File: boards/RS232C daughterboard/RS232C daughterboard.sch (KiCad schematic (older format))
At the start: 1 part

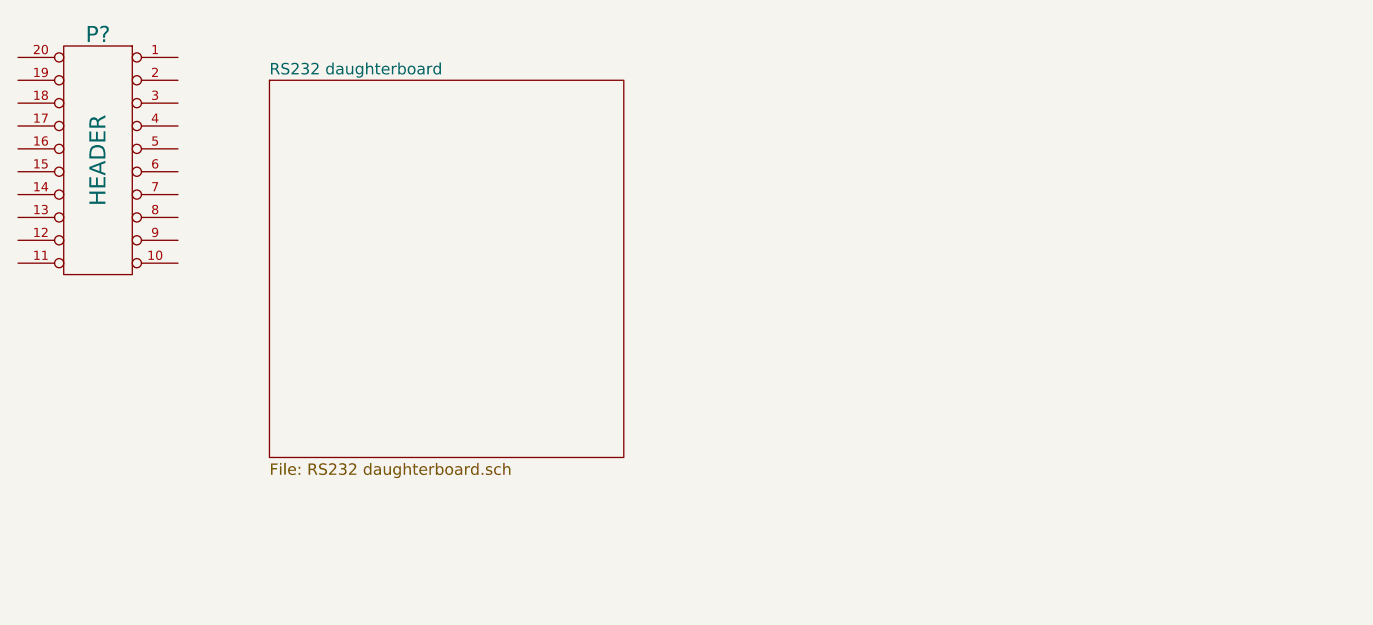
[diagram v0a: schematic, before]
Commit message: Filled in RS232 dboard, changed GPIO24 to GPIO16 board
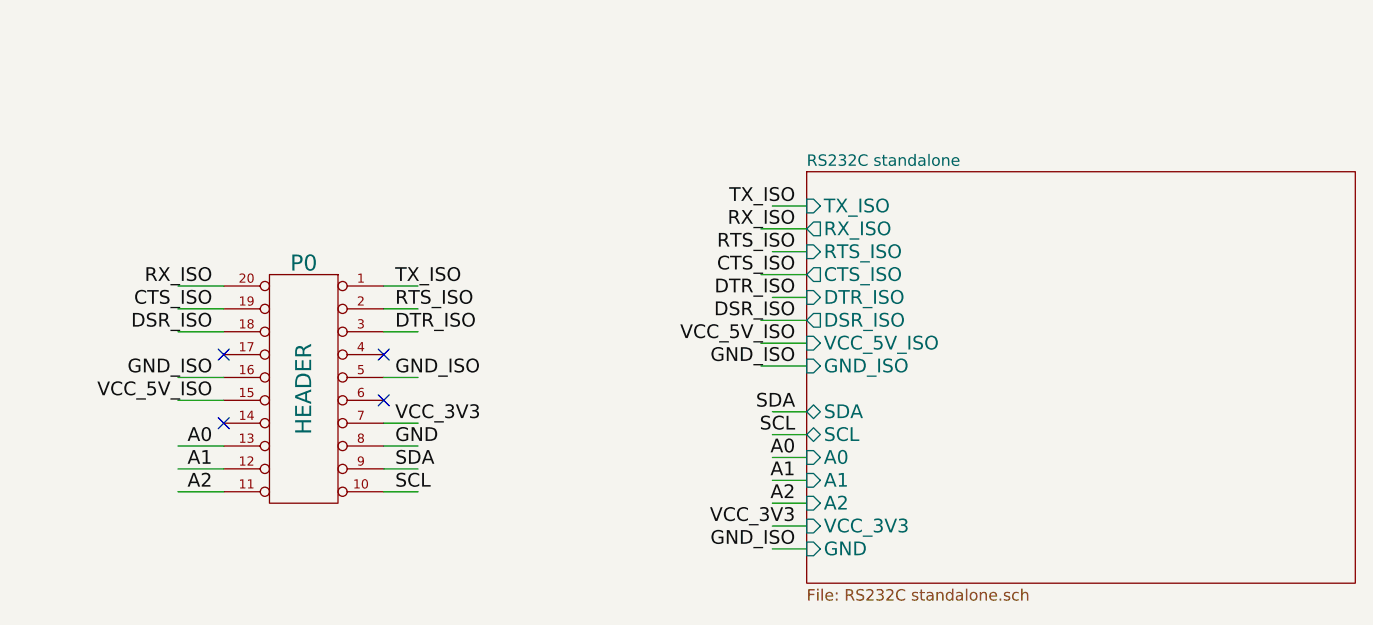
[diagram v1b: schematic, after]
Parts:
- removed P?: HEADER, symbol DIL20
- added P0: HEADER, symbol DIL20
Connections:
- net labels added: A0, A1, A2, CTS_ISO, DSR_ISO, DTR_ISO, GND, GND_ISO, RTS_ISO, RX_ISO, SCL, SDA, TX_ISO, VCC_3V3, VCC_5V_ISO
- wire segments 0 -> 31
- no-connect marks 0 -> 4
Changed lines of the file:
@@
 LIBS:CONN_16
 LIBS:csmall
+LIBS:ISL83387E
+LIBS:RS232C daughterboard-cache
 EELAYER 27 0
 EELAYER END
 $Descr A4 11693 8268
 encoding utf-8
-Sheet 1 1
+Sheet 1 2
 Title ""
 Date "26 jun 2014"
@@
 $EndDescr
 $Comp
-L DIL20 P?
-U 1 1 53AB657B
-P 2900 3300
-F 0 "P?" H 2900 3850 70  0000 C CNN
-F 1 "HEADER" V 2900 3300 70  0000 C CNN
-F 2 "" H 2900 3300 60  0000 C CNN
-F 3 "" H 2900 3300 60  0000 C CNN
-	1    2900 3300
+L DIL20 P0
+U 1 1 53AB69C0
+P 3800 4300
+F 0 "P0" H 3800 4850 70  0000 C CNN
+F 1 "HEADER" V 3800 4300 70  0000 C CNN
+F 2 "" H 3800 4300 60  0000 C CNN
+F 3 "" H 3800 4300 60  0000 C CNN
+	1    3800 4300
 	-1   0    0    -1
 $EndComp
 $Sheet
-S 3650 2950 1550 1650
-U 53AB65C8
-F0 "RS232 daughterboard" 50
-F1 "RS232 daughterboard.sch" 50
+S 6000 3350 2400 1800
+U 53AB69CE
+F0 "RS232C standalone" 50
+F1 "RS232C standalone.sch" 50
+F2 "TX_ISO" I L 6000 3500 60
+F3 "RX_ISO" O L 6000 3600 60
+F4 "RTS_ISO" I L 6000 3700 60
+F5 "CTS_ISO" O L 6000 3800 60
+F6 "DTR_ISO" I L 6000 3900 60
+F7 "DSR_ISO" O L 6000 4000 60
+F8 "VCC_3V3" I L 6000 4900 60
+F9 "GND" I L 6000 5000 60
+F10 "VCC_5V_ISO" I L 6000 4100 60
+F11 "GND_ISO" I L 6000 4200 60
+F12 "SDA" B L 6000 4400 60
+F13 "SCL" B L 6000 4500 60
+F14 "A0" I L 6000 4600 60
+F15 "A1" I L 6000 4700 60
+F16 "A2" I L 6000 4800 60
 $EndSheet
+Wire Wire Line
+	3450 3850 3250 3850
+Wire Wire Line
+	3450 3950 3250 3950
+Wire Wire Line
+	3450 4050 3250 4050
+Wire Wire Line
+	3450 4250 3250 4250
+Wire Wire Line
+	3450 4350 3250 4350
+Wire Wire Line
+	3450 4550 3250 4550
+Wire Wire Line
+	4300 3850 4150 3850
+Wire Wire Line
+	4300 3950 4150 3950
+Wire Wire Line
+	4300 4050 4150 4050
+Wire Wire Line
+	4300 4250 4150 4250
+Wire Wire Line
+	4300 4450 4150 4450
+Wire Wire Line
+	4300 4550 4150 4550
+Wire Wire Line
+	3450 4650 3250 4650
+Wire Wire Line
+	3450 4750 3250 4750
+Wire Wire Line
+	4300 4650 4150 4650
+Wire Wire Line
+	4300 4750 4150 4750
+Text Label 4200 3850 0    60   ~ 0
+TX_ISO
+Text Label 4200 3950 0    60   ~ 0
+RTS_ISO
+Text Label 4200 4050 0    60   ~ 0
+DTR_ISO
+Text Label 4200 4450 0    60   ~ 0
+VCC_3V3
+Text Label 4200 4550 0    60   ~ 0
+GND
+Text Label 4200 4650 0    60   ~ 0
+SDA
+Text Label 4200 4750 0    60   ~ 0
+SCL
+Text Label 3400 4750 2    60   ~ 0
+A2
+Text Label 3400 4650 2    60   ~ 0
+A1
+Text Label 3400 4550 2    60   ~ 0
+A0
+Text Label 3400 4350 2    60   ~ 0
+VCC_5V_ISO
+Text Label 3400 4250 2    60   ~ 0
+GND_ISO
+Text Label 3400 4050 2    60   ~ 0
+DSR_ISO
+Text Label 3400 3950 2    60   ~ 0
+CTS_ISO
+Text Label 3400 3850 2    60   ~ 0
+RX_ISO
+Text Label 4200 4250 0    60   ~ 0
+GND_ISO
+NoConn ~ 4150 4350
+NoConn ~ 4150 4150
+NoConn ~ 3450 4150
+NoConn ~ 3450 4450
+Wire Wire Line
+	6000 3600 5800 3600
+Text Label 5950 3600 2    60   ~ 0
+RX_ISO
+Wire Wire Line
+	6000 3800 5800 3800
+Text Label 5950 3800 2    60   ~ 0
+CTS_ISO
+Wire Wire Line
+	6000 4000 5800 4000
+Text Label 5950 4000 2    60   ~ 0
+DSR_ISO
+Wire Wire Line
+	5850 3500 6000 3500
+Text Label 5950 3500 2    60   ~ 0
+TX_ISO
+Wire Wire Line
+	5850 3700 6000 3700
+Wire Wire Line
+	5850 3900 6000 3900
+Text Label 5950 3700 2    60   ~ 0
+RTS_ISO
+Text Label 5950 3900 2    60   ~ 0
+DTR_ISO
+Wire Wire Line
+	6000 4100 5800 4100
+Text Label 5950 4100 2    60   ~ 0
+VCC_5V_ISO
+Wire Wire Line
+	6000 4200 5800 4200
+Text Label 5950 4200 2    60   ~ 0
+GND_ISO
+Wire Wire Line
+	6000 4600 5850 4600
+Wire Wire Line
+	6000 4700 5850 4700
+Wire Wire Line
+	6000 4800 5850 4800
+Text Label 5950 4800 2    60   ~ 0
+A2
+Text Label 5950 4700 2    60   ~ 0
+A1
+Text Label 5950 4600 2    60   ~ 0
+A0
+Wire Wire Line
+	5850 4400 6000 4400
+Wire Wire Line
+	5850 4500 6000 4500
+Text Label 5950 4400 2    60   ~ 0
+SDA
+Text Label 5950 4500 2    60   ~ 0
+SCL
+Wire Wire Line
+	5850 5000 6000 5000
+Text Label 5950 4900 2    60   ~ 0
+VCC_3V3
+Text Label 5950 5000 2    60   ~ 0
+GND_ISO
+Wire Wire Line
+	6000 4900 5850 4900
 $EndSCHEMATC

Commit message: Completed RS232C daughterboard
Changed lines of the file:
@@
 NoConn ~ 3450 4450
 Wire Wire Line
-	6000 3600 5800 3600
-Text Label 5950 3600 2    60   ~ 0
+	6000 3600 5850 3600
+Text Label 5850 3600 2    60   ~ 0
 RX_ISO
 Wire Wire Line
-	6000 3800 5800 3800
-Text Label 5950 3800 2    60   ~ 0
+	6000 3800 5850 3800
+Text Label 5850 3800 2    60   ~ 0
 CTS_ISO
 Wire Wire Line
-	6000 4000 5800 4000
-Text Label 5950 4000 2    60   ~ 0
+	6000 4000 5850 4000
+Text Label 5850 4000 2    60   ~ 0
 DSR_ISO
 Wire Wire Line
 	5850 3500 6000 3500
-Text Label 5950 3500 2    60   ~ 0
+Text Label 5850 3500 2    60   ~ 0
 TX_ISO
 Wire Wire Line
@@
 Wire Wire Line
 	5850 3900 6000 3900
-Text Label 5950 3700 2    60   ~ 0
+Text Label 5850 3700 2    60   ~ 0
 RTS_ISO
-Text Label 5950 3900 2    60   ~ 0
+Text Label 5850 3900 2    60   ~ 0
 DTR_ISO
 Wire Wire Line
-	6000 4100 5800 4100
-Text Label 5950 4100 2    60   ~ 0
+	6000 4100 5850 4100
+Text Label 5850 4100 2    60   ~ 0
 VCC_5V_ISO
 Wire Wire Line
-	6000 4200 5800 4200
-Text Label 5950 4200 2    60   ~ 0
+	6000 4200 5850 4200
+Text Label 5850 4200 2    60   ~ 0
 GND_ISO
 Wire Wire Line
@@
 Wire Wire Line
 	6000 4800 5850 4800
-Text Label 5950 4800 2    60   ~ 0
+Text Label 5850 4800 2    60   ~ 0
 A2
-Text Label 5950 4700 2    60   ~ 0
+Text Label 5850 4700 2    60   ~ 0
 A1
-Text Label 5950 4600 2    60   ~ 0
+Text Label 5850 4600 2    60   ~ 0
 A0
 Wire Wire Line
@@
 Wire Wire Line
 	5850 4500 6000 4500
-Text Label 5950 4400 2    60   ~ 0
+Text Label 5850 4400 2    60   ~ 0
 SDA
-Text Label 5950 4500 2    60   ~ 0
+Text Label 5850 4500 2    60   ~ 0
 SCL
 Wire Wire Line
 	5850 5000 6000 5000
-Text Label 5950 4900 2    60   ~ 0
+Text Label 5850 4900 2    60   ~ 0
 VCC_3V3
-Text Label 5950 5000 2    60   ~ 0
+Text Label 5850 5000 2    60   ~ 0
 GND_ISO
 Wire Wire Line

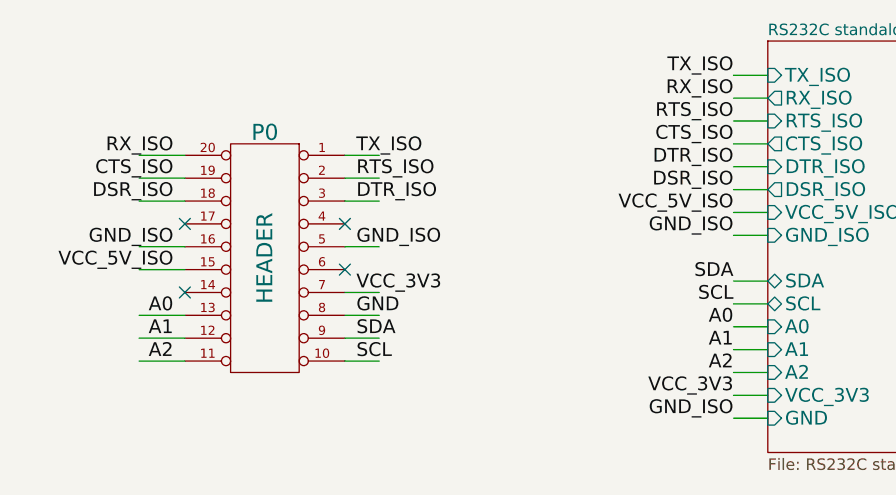
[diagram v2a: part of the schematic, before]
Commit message: Fixed errors in RS232C daughterboard, ERC passed
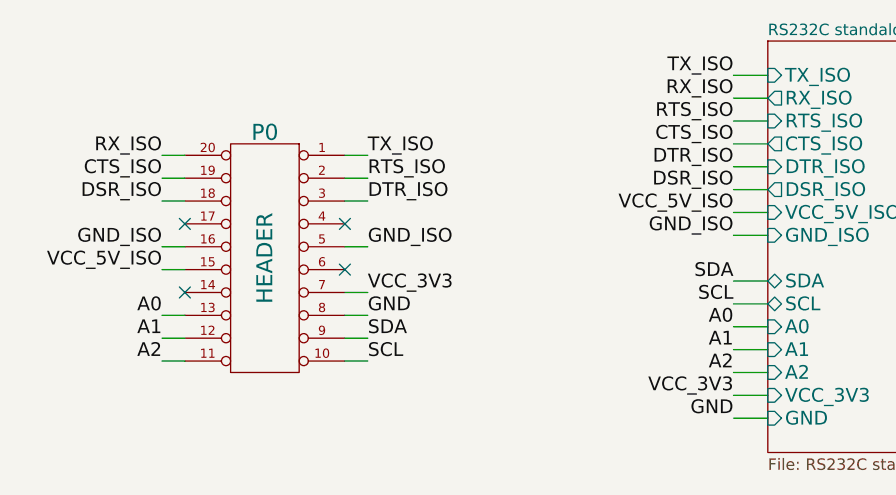
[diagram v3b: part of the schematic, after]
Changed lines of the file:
@@
 $EndSheet
 Wire Wire Line
-	3450 3850 3250 3850
+	3450 3850 3350 3850
 Wire Wire Line
-	3450 3950 3250 3950
+	3450 3950 3350 3950
 Wire Wire Line
-	3450 4050 3250 4050
+	3450 4050 3350 4050
 Wire Wire Line
-	3450 4250 3250 4250
+	3450 4250 3350 4250
 Wire Wire Line
-	3450 4350 3250 4350
+	3450 4350 3350 4350
 Wire Wire Line
-	3450 4550 3250 4550
+	3450 4550 3350 4550
 Wire Wire Line
-	4300 3850 4150 3850
+	4250 3850 4150 3850
 Wire Wire Line
-	4300 3950 4150 3950
+	4250 3950 4150 3950
 Wire Wire Line
-	4300 4050 4150 4050
+	4250 4050 4150 4050
 Wire Wire Line
-	4300 4250 4150 4250
+	4250 4250 4150 4250
 Wire Wire Line
-	4300 4450 4150 4450
+	4250 4450 4150 4450
 Wire Wire Line
-	4300 4550 4150 4550
+	4250 4550 4150 4550
 Wire Wire Line
-	3450 4650 3250 4650
+	3450 4650 3350 4650
 Wire Wire Line
-	3450 4750 3250 4750
+	3450 4750 3350 4750
 Wire Wire Line
-	4300 4650 4150 4650
+	4250 4650 4150 4650
 Wire Wire Line
-	4300 4750 4150 4750
-Text Label 4200 3850 0    60   ~ 0
+	4250 4750 4150 4750
+Text Label 4250 3850 0    60   ~ 0
 TX_ISO
-Text Label 4200 3950 0    60   ~ 0
+Text Label 4250 3950 0    60   ~ 0
 RTS_ISO
-Text Label 4200 4050 0    60   ~ 0
+Text Label 4250 4050 0    60   ~ 0
 DTR_ISO
-Text Label 4200 4450 0    60   ~ 0
+Text Label 4250 4450 0    60   ~ 0
 VCC_3V3
-Text Label 4200 4550 0    60   ~ 0
+Text Label 4250 4550 0    60   ~ 0
 GND
-Text Label 4200 4650 0    60   ~ 0
+Text Label 4250 4650 0    60   ~ 0
 SDA
-Text Label 4200 4750 0    60   ~ 0
+Text Label 4250 4750 0    60   ~ 0
 SCL
-Text Label 3400 4750 2    60   ~ 0
+Text Label 3350 4750 2    60   ~ 0
 A2
-Text Label 3400 4650 2    60   ~ 0
+Text Label 3350 4650 2    60   ~ 0
 A1
-Text Label 3400 4550 2    60   ~ 0
+Text Label 3350 4550 2    60   ~ 0
 A0
-Text Label 3400 4350 2    60   ~ 0
+Text Label 3350 4350 2    60   ~ 0
 VCC_5V_ISO
-Text Label 3400 4250 2    60   ~ 0
+Text Label 3350 4250 2    60   ~ 0
 GND_ISO
-Text Label 3400 4050 2    60   ~ 0
+Text Label 3350 4050 2    60   ~ 0
 DSR_ISO
-Text Label 3400 3950 2    60   ~ 0
+Text Label 3350 3950 2    60   ~ 0
 CTS_ISO
-Text Label 3400 3850 2    60   ~ 0
+Text Label 3350 3850 2    60   ~ 0
 RX_ISO
-Text Label 4200 4250 0    60   ~ 0
+Text Label 4250 4250 0    60   ~ 0
 GND_ISO
 NoConn ~ 4150 4350
@@
 VCC_3V3
 Text Label 5850 5000 2    60   ~ 0
-GND_ISO
+GND
 Wire Wire Line
 	6000 4900 5850 4900
